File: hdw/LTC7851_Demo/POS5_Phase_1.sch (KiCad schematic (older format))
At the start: 36 parts, among them U301 LTC7851UHH, U401 SiC779

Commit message: Assigned footprints
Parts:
- C401, C402, C403, C404, C406, C409, C411, C413, C414, C415: footprint (none) -> Capacitors_SMD:C_0603
- C405, C407, C408, C410, C412, C420: footprint (none) -> Capacitors_Tantalum_SMD:CP_Tantalum_Case-B_EIA-3528-21_Reflow
- C416, C417, C418, C419: footprint (none) -> Capacitors_SMD:C_1210
- L401: footprint (none) -> Inductors_SMD:L_Vishay_IHLP-4040
- R401, R402, R403, R404, R405, R406, R407, R408, R409, R410, R411: footprint (none) -> Resistors_SMD:R_0603
- TP401, TP402: footprint (none) -> Measurement_Points:Measurement_Point_Round-SMD-Pad_Small
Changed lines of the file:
@@
 F 0 "C409" H 4585 1440 50  0000 L CNN
 F 1 "1uF" H 4585 1240 50  0000 L CNN
-F 2 "" H 4598 1190 50  0001 C CNN
+F 2 "Capacitors_SMD:C_0603" H 4598 1190 50  0001 C CNN
 F 3 "" H 4585 1440 50  0001 C CNN
 F 4 "0603" H 4410 1440 50  0000 R CNN "display_footprint"
@@
 F 0 "TP401" V 5430 2960 50  0000 L CNN
 F 1 "TP" H 5430 2960 50  0001 C CNN
-F 2 "" H 5430 2810 60  0000 C CNN
+F 2 "Measurement_Points:Measurement_Point_Round-SMD-Pad_Small" H 5430 2810 60  0001 C CNN
 F 3 "" H 5430 2810 60  0000 C CNN
 	1    5430 2810
@@
 F 0 "TP402" V 5430 3060 50  0000 L CNN
 F 1 "TP" H 5430 3060 50  0001 C CNN
-F 2 "" H 5430 2910 60  0000 C CNN
+F 2 "Measurement_Points:Measurement_Point_Round-SMD-Pad_Small" H 5430 2910 60  0001 C CNN
 F 3 "" H 5430 2910 60  0000 C CNN
 	1    5430 2910
@@
 F 0 "L401" V 7390 3310 50  0000 C CNN
 F 1 "0.47uH" V 7515 3310 50  0000 C CNN
-F 2 "" H 7440 3310 50  0001 C CNN
+F 2 "Inductors_SMD:L_Vishay_IHLP-4040" H 7440 3310 50  0001 C CNN
 F 3 "" H 7440 3310 50  0001 C CNN
 F 4 "541-2595-1-ND" H 7440 3310 50  0001 C CNN "Digi-Key PN"
@@
 F 0 "R406" H 6880 2470 50  0000 R CNN
 F 1 "2" V 6980 2470 50  0000 C CNN
-F 2 "" H 6980 2470 50  0001 C CNN
+F 2 "Resistors_SMD:R_0603" H 6980 2470 50  0001 C CNN
 F 3 "" H 6980 2470 50  0001 C CNN
 F 4 "RMCF0603FT2R00CT-ND" H 7280 2870 60  0001 C CNN "Digi-Key PN"
@@
 F 0 "C413" H 7005 2950 50  0000 L CNN
 F 1 "0.1uF" H 7005 2750 50  0000 L CNN
-F 2 "" H 7018 2700 50  0001 C CNN
+F 2 "Capacitors_SMD:C_0603" H 7018 2700 50  0001 C CNN
 F 3 "" H 7005 2950 50  0001 C CNN
 F 4 "0603" H 6830 2950 50  0000 R CNN "display_footprint"
@@
 F 0 "R407" H 7290 3920 50  0000 L CNN
 F 1 "1.4k" V 7190 3770 40  0000 C CNN
-F 2 "" H 7190 3770 50  0001 C CNN
+F 2 "Resistors_SMD:R_0603" H 7190 3770 50  0001 C CNN
 F 3 "" H 7190 3770 50  0001 C CNN
 F 4 "P1.40KHCT-ND" H 7490 4170 60  0001 C CNN "Digi-Key PN"
@@
 F 0 "C415" V 6916 4040 50  0000 C CNN
 F 1 "0.22uF" V 7007 3910 50  0000 L CNN
-F 2 "" H 7478 3890 50  0001 C CNN
+F 2 "Capacitors_SMD:C_0603" H 7478 3890 50  0001 C CNN
 F 3 "" H 7465 4140 50  0001 C CNN
 F 4 "490-5402-1-ND" H 7865 4540 60  0001 C CNN "Digi-Key PN"
@@
 F 0 "C416" H 7905 1440 50  0000 L CNN
 F 1 "22uF" H 7905 1240 50  0000 L CNN
-F 2 "" H 7918 1190 50  0001 C CNN
+F 2 "Capacitors_SMD:C_1210" H 7918 1190 50  0001 C CNN
 F 3 "" H 7905 1440 50  0001 C CNN
 F 4 "445-1436-1-ND" H 8305 1840 60  0001 C CNN "Digi-Key PN"
@@
 F 0 "C417" H 8445 3640 50  0000 L CNN
 F 1 "100uF" H 8445 3440 50  0000 L CNN
-F 2 "" H 8458 3390 50  0001 C CNN
+F 2 "Capacitors_SMD:C_1210" H 8458 3390 50  0001 C CNN
 F 3 "" H 8445 3640 50  0001 C CNN
 F 4 "1210" H 8270 3640 50  0000 R CNN "display_footprint"
@@
 F 0 "R410" H 7840 5110 50  0000 R CNN
 F 1 "100k" V 7940 5110 40  0000 C CNN
-F 2 "" H 7940 5110 50  0001 C CNN
+F 2 "Resistors_SMD:R_0603" H 7940 5110 50  0001 C CNN
 F 3 "" H 7940 5110 50  0001 C CNN
 F 4 "P100KHCT-ND" H 8240 5510 60  0001 C CNN "Digi-Key PN"
@@
 F 0 "C404" H 3335 5480 50  0000 L CNN
 F 1 "2200pF" H 3335 5280 50  0000 L CNN
-F 2 "" H 3348 5230 50  0001 C CNN
+F 2 "Capacitors_SMD:C_0603" H 3348 5230 50  0001 C CNN
 F 3 "" H 3335 5480 50  0001 C CNN
 F 4 "0603" H 3160 5480 50  0000 R CNN "display_footprint"
@@
 F 0 "C406" H 3875 5710 50  0000 L CNN
 F 1 "100pF" H 3875 5510 50  0000 L CNN
-F 2 "" H 3888 5460 50  0001 C CNN
+F 2 "Capacitors_SMD:C_0603" H 3888 5460 50  0001 C CNN
 F 3 "" H 3875 5710 50  0001 C CNN
 F 4 "0603" H 3700 5710 50  0000 R CNN "display_footprint"
@@
 F 0 "C403" H 3335 4420 50  0000 L CNN
 F 1 "3300pF" H 3335 4220 50  0000 L CNN
-F 2 "" H 3348 4170 50  0001 C CNN
+F 2 "Capacitors_SMD:C_0603" H 3348 4170 50  0001 C CNN
 F 3 "" H 3335 4420 50  0001 C CNN
 F 4 "0603" H 3160 4420 50  0000 R CNN "display_footprint"
@@
 F 0 "R401" H 1610 6340 50  0000 R CNN
 F 1 "66.5k" V 1710 6340 40  0000 C CNN
-F 2 "" H 1710 6340 50  0001 C CNN
+F 2 "Resistors_SMD:R_0603" H 1710 6340 50  0001 C CNN
 F 3 "" H 1710 6340 50  0001 C CNN
 F 4 "RMCF0603FT66K5CT-ND" H 2010 6740 60  0001 C CNN "Digi-Key PN"
@@
 F 0 "C411" H 5205 1970 50  0000 L CNN
 F 1 "0.1uF" H 5205 1770 50  0000 L CNN
-F 2 "" H 5218 1720 50  0001 C CNN
+F 2 "Capacitors_SMD:C_0603" H 5218 1720 50  0001 C CNN
 F 3 "" H 5205 1970 50  0001 C CNN
 F 4 "0603" H 5030 1970 50  0000 R CNN "display_footprint"
@@
 F 0 "R405" H 5080 1340 50  0000 R CNN
 F 1 "2" V 5180 1340 50  0000 C CNN
-F 2 "" H 5180 1340 50  0001 C CNN
+F 2 "Resistors_SMD:R_0603" H 5180 1340 50  0001 C CNN
 F 3 "" H 5180 1340 50  0001 C CNN
 F 4 "RMCF0603FT2R00CT-ND" H 5480 1740 60  0001 C CNN "Digi-Key PN"
@@
 F 0 "R409" H 7840 4730 50  0000 R CNN
 F 1 "10" V 7940 4730 50  0000 C CNN
-F 2 "" H 7940 4730 50  0001 C CNN
+F 2 "Resistors_SMD:R_0603" H 7940 4730 50  0001 C CNN
 F 3 "" H 7940 4730 50  0001 C CNN
 F 4 "YAG3351CT-ND" H 8240 5130 60  0001 C CNN "Digi-Key PN"
@@
 F 0 "C414" H 7305 1440 50  0000 L CNN
 F 1 "1uF" H 7305 1240 50  0000 L CNN
-F 2 "" H 7318 1190 50  0001 C CNN
+F 2 "Capacitors_SMD:C_0603" H 7318 1190 50  0001 C CNN
 F 3 "" H 7305 1440 50  0001 C CNN
 F 4 "0603" H 7130 1440 50  0000 R CNN "display_footprint"
@@
 F 0 "C420" H 9645 3640 50  0000 L CNN
 F 1 "100uF" H 9645 3440 50  0000 L CNN
-F 2 "" H 9658 3390 50  0001 C CNN
+F 2 "Capacitors_Tantalum_SMD:CP_Tantalum_Case-B_EIA-3528-21_Reflow" H 9658 3390 50  0001 C CNN
 F 3 "" H 9645 3640 50  0001 C CNN
 F 4 "478-9994-1-ND" H 9620 3540 50  0001 C CNN "Digi-Key PN"
@@
 F 0 "C419" H 9045 3640 50  0000 L CNN
 F 1 "100uF" H 9045 3440 50  0000 L CNN
-F 2 "" H 9058 3390 50  0001 C CNN
+F 2 "Capacitors_SMD:C_1210" H 9058 3390 50  0001 C CNN
 F 3 "" H 9045 3640 50  0001 C CNN
 F 4 "587-3432-1-ND" H 9445 4040 60  0001 C CNN "Digi-Key PN"
@@
 F 0 "C418" H 8505 1440 50  0000 L CNN
 F 1 "22uF" H 8505 1240 50  0000 L CNN
-F 2 "" H 8518 1190 50  0001 C CNN
+F 2 "Capacitors_SMD:C_1210" H 8518 1190 50  0001 C CNN
 F 3 "" H 8505 1440 50  0001 C CNN
 F 4 "445-1436-1-ND" H 8905 1840 60  0001 C CNN "Digi-Key PN"
@@
 F 0 "C405" H 3355 7470 50  0000 L CNN
 F 1 "100uF" H 3355 7270 50  0000 L CNN
-F 2 "" H 3368 7220 50  0001 C CNN
+F 2 "Capacitors_Tantalum_SMD:CP_Tantalum_Case-B_EIA-3528-21_Reflow" H 3368 7220 50  0001 C CNN
 F 3 "" H 3355 7470 50  0001 C CNN
 F 4 "478-9994-1-ND" H 3330 7370 50  0001 C CNN "Digi-Key PN"
@@
 F 0 "C407" H 3955 7470 50  0000 L CNN
 F 1 "100uF" H 3955 7270 50  0000 L CNN
-F 2 "" H 3968 7220 50  0001 C CNN
+F 2 "Capacitors_Tantalum_SMD:CP_Tantalum_Case-B_EIA-3528-21_Reflow" H 3968 7220 50  0001 C CNN
 F 3 "" H 3955 7470 50  0001 C CNN
 F 4 "478-9994-1-ND" H 3930 7370 50  0001 C CNN "Digi-Key PN"
@@
 F 0 "C408" H 4555 7470 50  0000 L CNN
 F 1 "100uF" H 4555 7270 50  0000 L CNN
-F 2 "" H 4568 7220 50  0001 C CNN
+F 2 "Capacitors_Tantalum_SMD:CP_Tantalum_Case-B_EIA-3528-21_Reflow" H 4568 7220 50  0001 C CNN
 F 3 "" H 4555 7470 50  0001 C CNN
 F 4 "478-9994-1-ND" H 4530 7370 50  0001 C CNN "Digi-Key PN"
@@
 F 0 "C410" H 5155 7470 50  0000 L CNN
 F 1 "100uF" H 5155 7270 50  0000 L CNN
-F 2 "" H 5168 7220 50  0001 C CNN
+F 2 "Capacitors_Tantalum_SMD:CP_Tantalum_Case-B_EIA-3528-21_Reflow" H 5168 7220 50  0001 C CNN
 F 3 "" H 5155 7470 50  0001 C CNN
 F 4 "478-9994-1-ND" H 5130 7370 50  0001 C CNN "Digi-Key PN"
@@
 F 0 "C412" H 5755 7470 50  0000 L CNN
 F 1 "100uF" H 5755 7270 50  0000 L CNN
-F 2 "" H 5768 7220 50  0001 C CNN
+F 2 "Capacitors_Tantalum_SMD:CP_Tantalum_Case-B_EIA-3528-21_Reflow" H 5768 7220 50  0001 C CNN
 F 3 "" H 5755 7470 50  0001 C CNN
 F 4 "478-9994-1-ND" H 5730 7370 50  0001 C CNN "Digi-Key PN"
@@
 F 0 "R411" H 7840 5580 50  0000 R CNN
 F 1 "13.7k" V 7940 5580 40  0000 C CNN
-F 2 "" H 7940 5580 50  0001 C CNN
+F 2 "Resistors_SMD:R_0603" H 7940 5580 50  0001 C CNN
 F 3 "" H 7940 5580 50  0001 C CNN
 F 4 "P13.7KHCT-ND" H 8240 5980 60  0001 C CNN "Digi-Key PN"
@@
 F 0 "R404" H 3750 4620 50  0000 R CNN
 F 1 "10k" V 3850 4620 50  0000 C CNN
-F 2 "" H 3850 4620 50  0001 C CNN
+F 2 "Resistors_SMD:R_0603" H 3850 4620 50  0001 C CNN
 F 3 "" H 3850 4620 50  0001 C CNN
 F 4 "RHM10KADCT-ND" H 4150 5020 60  0001 C CNN "Digi-Key PN"
@@
 F 0 "R402" H 3210 4780 50  0000 R CNN
 F 1 "320" V 3310 4780 50  0000 C CNN
-F 2 "" H 3310 4780 50  0001 C CNN
+F 2 "Resistors_SMD:R_0603" H 3310 4780 50  0001 C CNN
 F 3 "" H 3310 4780 50  0001 C CNN
 F 4 "541-4544-1-ND" H 3610 5180 60  0001 C CNN "Digi-Key PN"
@@
 F 0 "R403" H 3210 5840 50  0000 R CNN
 F 1 "6.04k" V 3310 5840 40  0000 C CNN
-F 2 "" H 3310 5840 50  0001 C CNN
+F 2 "Resistors_SMD:R_0603" H 3310 5840 50  0001 C CNN
 F 3 "" H 3310 5840 50  0001 C CNN
 F 4 "311-6.04KHRCT-ND" H 3610 6240 60  0001 C CNN "Digi-Key PN"
@@
 F 0 "C402" H 1735 5840 50  0000 L CNN
 F 1 "100pF" H 1735 5640 50  0000 L CNN
-F 2 "" H 1748 5590 50  0001 C CNN
+F 2 "Capacitors_SMD:C_0603" H 1748 5590 50  0001 C CNN
 F 3 "" H 1735 5840 50  0001 C CNN
 F 4 "0603" H 1560 5840 50  0000 R CNN "display_footprint"
@@
 F 0 "C401" H 1735 5240 50  0000 L CNN
 F 1 "100pF" H 1735 5040 50  0000 L CNN
-F 2 "" H 1748 4990 50  0001 C CNN
+F 2 "Capacitors_SMD:C_0603" H 1748 4990 50  0001 C CNN
 F 3 "" H 1735 5240 50  0001 C CNN
 F 4 "0603" H 1560 5240 50  0000 R CNN "display_footprint"
@@
 F 0 "R408" V 7290 5810 50  0000 C CNN
 F 1 "0" V 7680 5810 50  0000 C CNN
-F 2 "" H 7680 5810 50  0001 C CNN
+F 2 "Resistors_SMD:R_0603" H 7680 5810 50  0001 C CNN
 F 3 "" H 7680 5810 50  0001 C CNN
 F 4 "0603" V 7383 5810 50  0000 C CNN "display_footprint"

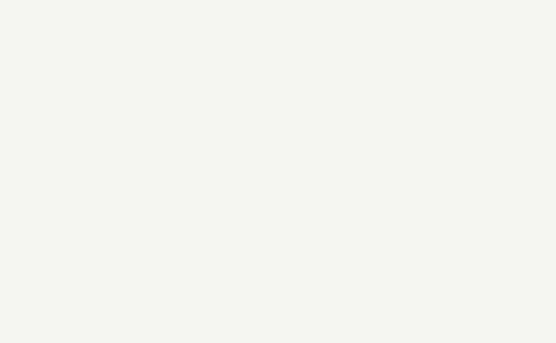
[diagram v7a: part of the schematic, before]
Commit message: Added page titles
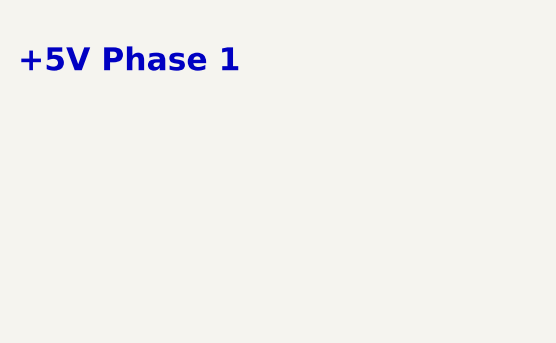
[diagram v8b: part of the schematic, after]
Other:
- note added: "+5V Phase 1"
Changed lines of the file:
@@
 	6810 4110 6810 4010
 Connection ~ 6810 4010
+Text Notes 540  690  0    100  ~ 20
++5V Phase 1
 $EndSCHEMATC
